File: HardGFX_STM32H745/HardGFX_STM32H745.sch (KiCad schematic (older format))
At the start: 16 parts, among them SW2 SW_MEC_5E, U1 STM32H745BIT3, X1 XO32, Y1 ECS-.327-6-34R-TR

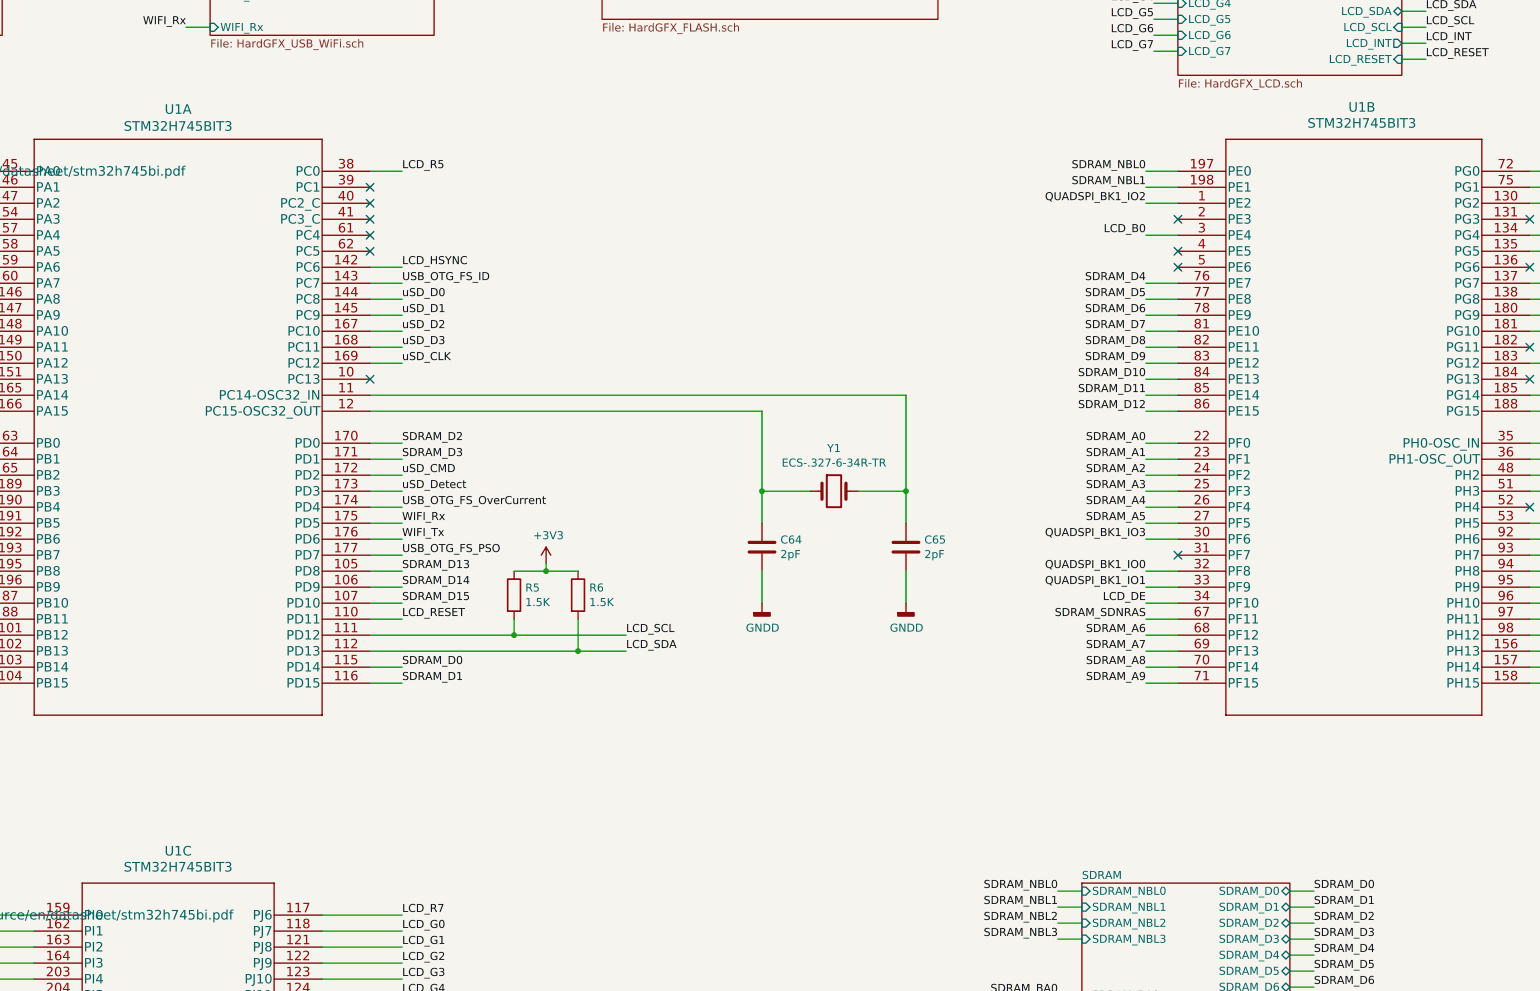
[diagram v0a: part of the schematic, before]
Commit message: Add Info folder that contain data about reference design, datasheet component of references.
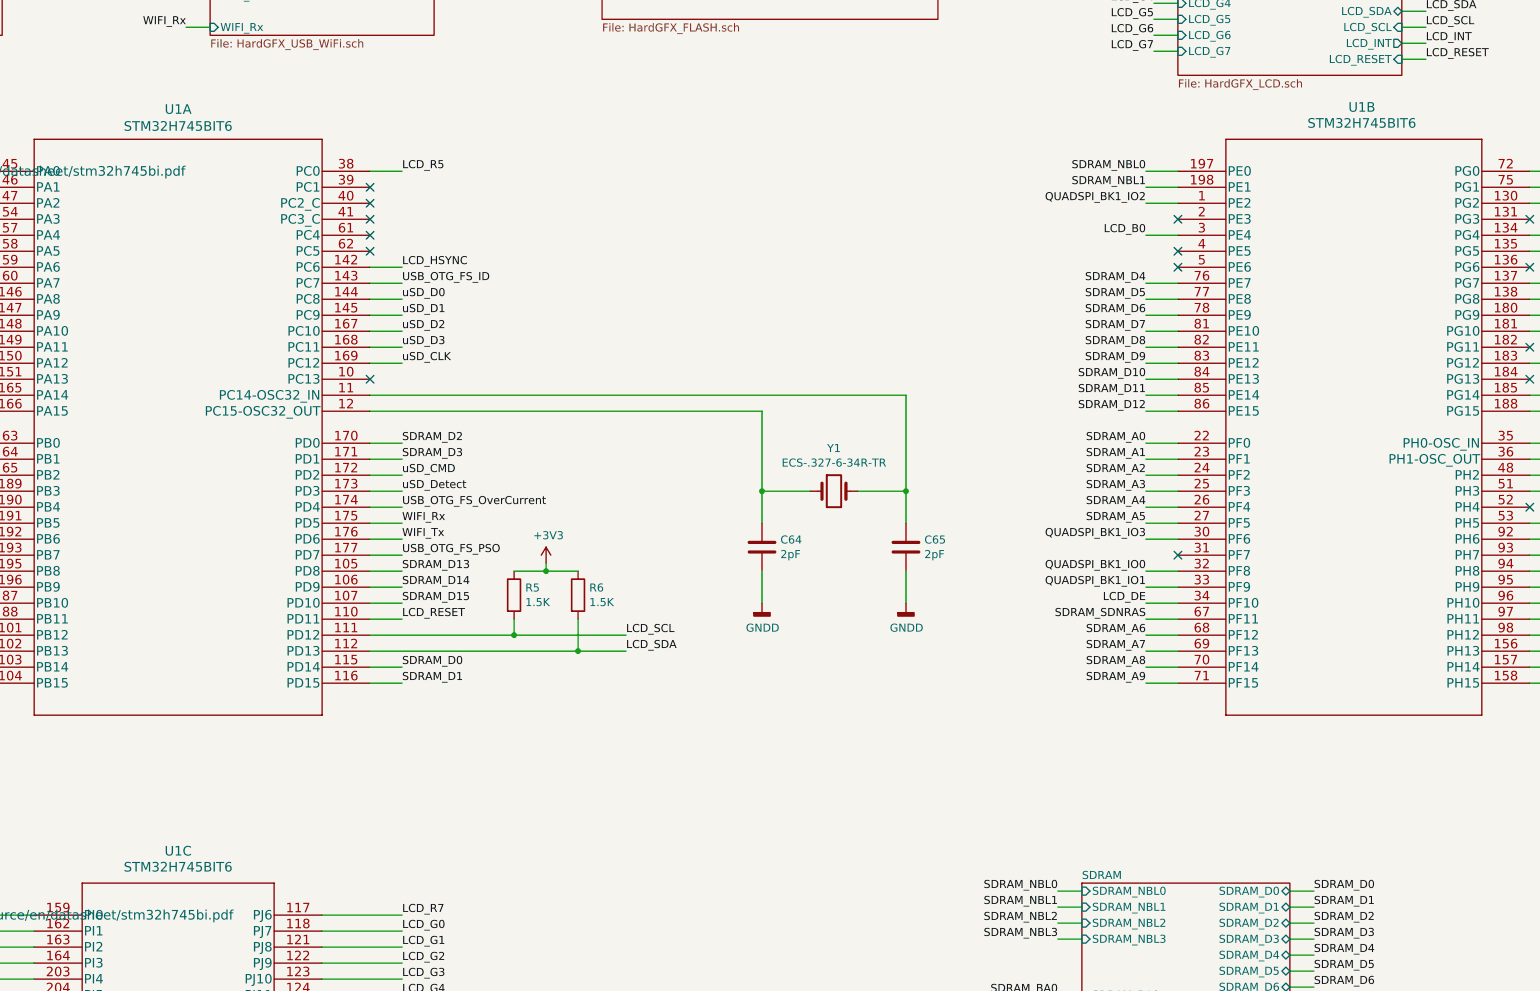
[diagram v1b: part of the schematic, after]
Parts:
- U1: value STM32H745BIT3 -> STM32H745BIT6; Digikey# (none) -> STM32H745BIT6-ND; MANUFACTURER (none) -> STMicroelectronics; Manf# (none) -> STM32H745BIT6
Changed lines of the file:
@@
 P 2650 3300
 F 0 "U1" H 3850 3687 60  0000 C CNN
-F 1 "STM32H745BIT3" H 3850 3581 60  0000 C CNN
+F 1 "STM32H745BIT6" H 3850 3581 60  0000 C CNN
 F 2 "STM32H745BIT3:STM32H745BIT3" H 3850 3540 60  0001 C CNN
 F 3 "https://www.st.com/resource/en/datasheet/stm32h745bi.pdf" H 2650 3300 60  0000 C CNN
+F 4 "STM32H745BIT6" H 2650 3300 50  0001 C CNN "Manf#"
+F 5 "STM32H745BIT6-ND" H 2650 3300 50  0001 C CNN "Digikey#"
+F 6 "STMicroelectronics" H 2650 3300 50  0001 C CNN "MANUFACTURER"
 	1    2650 3300
 	1    0    0    -1
@@
 P 2950 7950
 F 0 "U1" H 3850 8350 60  0000 C CNN
-F 1 "STM32H745BIT3" H 3850 8250 60  0000 C CNN
+F 1 "STM32H745BIT6" H 3850 8250 60  0000 C CNN
 F 2 "STM32H745BIT3:STM32H745BIT3" H 4150 8190 60  0001 C CNN
 F 3 "https://www.st.com/resource/en/datasheet/stm32h745bi.pdf" H 2950 7950 60  0000 C CNN
+F 4 "STM32H745BIT6" H 2950 7950 50  0001 C CNN "Manf#"
+F 5 "STM32H745BIT6-ND" H 2950 7950 50  0001 C CNN "Digikey#"
+F 6 "STMicroelectronics" H 2950 7950 50  0001 C CNN "MANUFACTURER"
 	3    2950 7950
 	1    0    0    -1
@@
 P 10100 3300
 F 0 "U1" H 11250 3700 60  0000 C CNN
-F 1 "STM32H745BIT3" H 11250 3600 60  0000 C CNN
+F 1 "STM32H745BIT6" H 11250 3600 60  0000 C CNN
 F 2 "STM32H745BIT3:STM32H745BIT3" H 11300 3540 60  0001 C CNN
 F 3 "https://www.st.com/resource/en/datasheet/stm32h745bi.pdf" H 10100 3300 60  0001 C CNN
+F 4 "STM32H745BIT6" H 10100 3300 50  0001 C CNN "Manf#"
+F 5 "STM32H745BIT6-ND" H 10100 3300 50  0001 C CNN "Digikey#"
+F 6 "STMicroelectronics" H 10100 3300 50  0001 C CNN "MANUFACTURER"
 	2    10100 3300
 	1    0    0    -1
